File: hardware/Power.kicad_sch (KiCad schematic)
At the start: 24 parts, among them J200 Conn_Receptacle_2P, Q200 AO3401A, U200 RT9080-33GJ5, U201 TPS61023DRLR, U202 MCP73831-2-OT, X200 12401598E4#2A

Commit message: Add buttons to PCB layout
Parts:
- added SW200, SW201: SW_Push_Dual, SMD_SW_6mm:SW_Push_1P1T_NO_6x6mm_H9.5mm, symbol Switch:SW_Push_Dual
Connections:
- net GND: now also SW200.1, SW200.3, SW201.1, SW201.3
- new net JOY_BACK: SW200.2, SW200.4
- new net JOY_HOME: SW201.2, SW201.4
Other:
- note added: "User input"
- moved on the sheet: C205, R208, U202

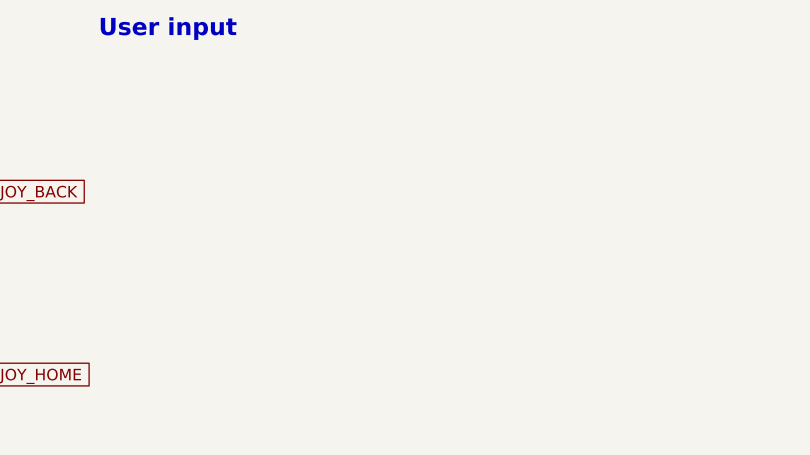
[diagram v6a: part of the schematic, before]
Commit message: Add joystick to PCB
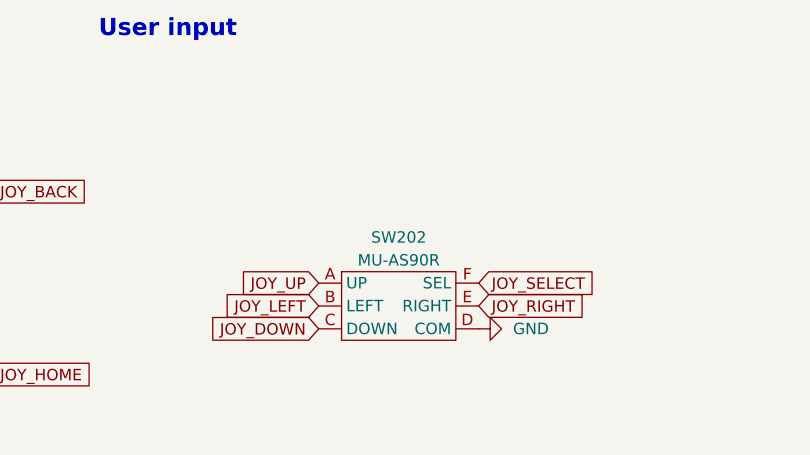
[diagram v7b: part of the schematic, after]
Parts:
- added SW202: MU-AS90R, MU-AS90R:MU-AS90R, symbol MU-AS90R:MU-AS90R
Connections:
- net GND: now also SW202.D (COM)
- new net JOY_DOWN: SW202.C (DOWN)
- new net JOY_LEFT: SW202.B (LEFT)
- new net JOY_RIGHT: SW202.E (RIGHT)
- new net JOY_SELECT: SW202.F (SEL)
- new net JOY_UP: SW202.A (UP)
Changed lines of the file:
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@@
 		)
 	)
+	(global_label "JOY_RIGHT"
+		(shape input)
+		(at 104.14 173.99 0)
+		(fields_autoplaced yes)
+		(effects
+			(font
+				(size 1.27 1.27)
+			)
+			(justify left)
+		)
+		(property "Intersheetrefs" "${INTERSHEET_REFS}"
+			(at 116.9224 173.99 0)
+			(effects
+				(font
+					(size 1.27 1.27)
+				)
+				(justify left)
+				(hide yes)
+			)
+		)
+	)
 	(global_label "JOY_BACK"
 		(shape input)
@@
 		)
 	)
+	(global_label "JOY_LEFT"
+		(shape input)
+		(at 86.36 173.99 180)
+		(fields_autoplaced yes)
+		(effects
+			(font
+				(size 1.27 1.27)
+			)
+			(justify right)
+		)
+		(property "Intersheetrefs" "${INTERSHEET_REFS}"
+			(at 86.36 173.99 0)
+			(effects
+				(font
+					(size 1.27 1.27)
+				)
+				(hide yes)
+			)
+		)
+	)
 	(global_label "USB_D-"
 		(shape input)
@@
 		)
 	)
+	(global_label "JOY_DOWN"
+		(shape input)
+		(at 86.36 176.53 180)
+		(fields_autoplaced yes)
+		(effects
+			(font
+				(size 1.27 1.27)
+			)
+			(justify right)
+		)
+		(property "Intersheetrefs" "${INTERSHEET_REFS}"
+			(at 86.36 176.53 0)
+			(effects
+				(font
+					(size 1.27 1.27)
+				)
+				(hide yes)
+			)
+		)
+	)
 	(global_label "5V_EN"
 		(shape input)
@@
 		)
 	)
+	(global_label "JOY_UP"
+		(shape input)
+		(at 86.36 171.45 180)
+		(fields_autoplaced yes)
+		(effects
+			(font
+				(size 1.27 1.27)
+			)
+			(justify right)
+		)
+		(property "Intersheetrefs" "${INTERSHEET_REFS}"
+			(at 86.36 171.45 0)
+			(effects
+				(font
+					(size 1.27 1.27)
+				)
+				(hide yes)
+			)
+		)
+	)
+	(global_label "JOY_SELECT"
+		(shape input)
+		(at 104.14 171.45 0)
+		(fields_autoplaced yes)
+		(effects
+			(font
+				(size 1.27 1.27)
+			)
+			(justify left)
+		)
+		(property "Intersheetrefs" "${INTERSHEET_REFS}"
+			(at 104.14 171.45 0)
+			(effects
+				(font
+					(size 1.27 1.27)
+				)
+				(hide yes)
+			)
+		)
+	)
 	(global_label "USB_D-"
 		(shape input)
@@
 	)
 	(symbol
+		(lib_id "MU-AS90R:MU-AS90R")
+		(at 95.25 166.37 0)
+		(unit 1)
+		(exclude_from_sim no)
+		(in_bom yes)
+		(on_board yes)
+		(dnp no)
+		(fields_autoplaced yes)
+		(property "Reference" "SW202"
+			(at 95.25 166.37 0)
+			(effects
+				(font
+					(size 1.27 1.27)
+				)
+			)
+		)
+		(property "Value" "MU-AS90R"
+			(at 95.25 168.91 0)
+			(effects
+				(font
+					(size 1.27 1.27)
+				)
+			)
+		)
+		(property "Footprint" "MU-AS90R:MU-AS90R"
+			(at 95.25 166.37 0)
+			(effects
+				(font
+					(size 1.27 1.27)
+				)
+				(hide yes)
+			)
+		)
+		(property "Datasheet" ""
+			(at 95.25 166.37 0)
+			(effects
+				(font
+					(size 1.27 1.27)
+				)
+				(hide yes)
+			)
+		)
+		(property "Description" ""
+			(at 95.25 166.37 0)
+			(effects
+				(font
+					(size 1.27 1.27)
+				)
+				(hide yes)
+			)
+		)
+		(pin "F"
+		)
+		(pin "E"
+		)
+		(pin "A"
+		)
+		(pin "D"
+		)
+		(pin "C"
+		)
+		(pin "B"
+		)
+		(instances
+			(project ""
+				(path "/da54d175-8762-4f8c-be46-30694592bf7b/f250b6aa-fac8-4faa-af78-57e6d3c4eae4"
+					(reference "SW202")
+					(unit 1)
+				)
+			)
+		)
+	)
+	(symbol
 		(lib_id "power:GND")
 		(at 60.325 55.88 90)
@@
 					(unit 1)
 				)
+			)
+		)
+	)
+	(symbol
+		(lib_name "GND_5")
+		(lib_id "power:GND")
+		(at 104.14 176.53 90)
+		(unit 1)
+		(exclude_from_sim no)
+		(in_bom yes)
+		(on_board yes)
+		(dnp no)
+		(fields_autoplaced yes)
+		(property "Reference" "#PWR0203"
+			(at 110.49 176.53 0)
+			(effects
+				(font
+					(size 1.27 1.27)
+				)
+				(hide yes)
+			)
+		)
+		(property "Value" "GND"
+			(at 107.95 176.5299 90)
+			(effects
+				(font
+					(size 1.27 1.27)
+				)
+				(justify right)
+			)
+		)
+		(property "Footprint" ""
+			(at 104.14 176.53 0)
+			(effects
+				(font
+					(size 1.27 1.27)
+				)
+				(hide yes)
+			)
+		)
+		(property "Datasheet" ""
+			(at 104.14 176.53 0)
+			(effects
+				(font
+					(size 1.27 1.27)
+				)
+				(hide yes)
+			)
+		)
+		(property "Description" "Power symbol creates a global label with name \"GND\" , ground"
+			(at 104.14 176.53 0)
+			(effects
+				(font
+					(size 1.27 1.27)
+				)
+				(hide yes)
+			)
+		)
+		(pin "1"
+		)
+		(instances
+			(project "DigiCron"
+				(path "/da54d175-8762-4f8c-be46-30694592bf7b/f250b6aa-fac8-4faa-af78-57e6d3c4eae4"
+					(reference "#PWR0203")
+					(unit 1)
+				)

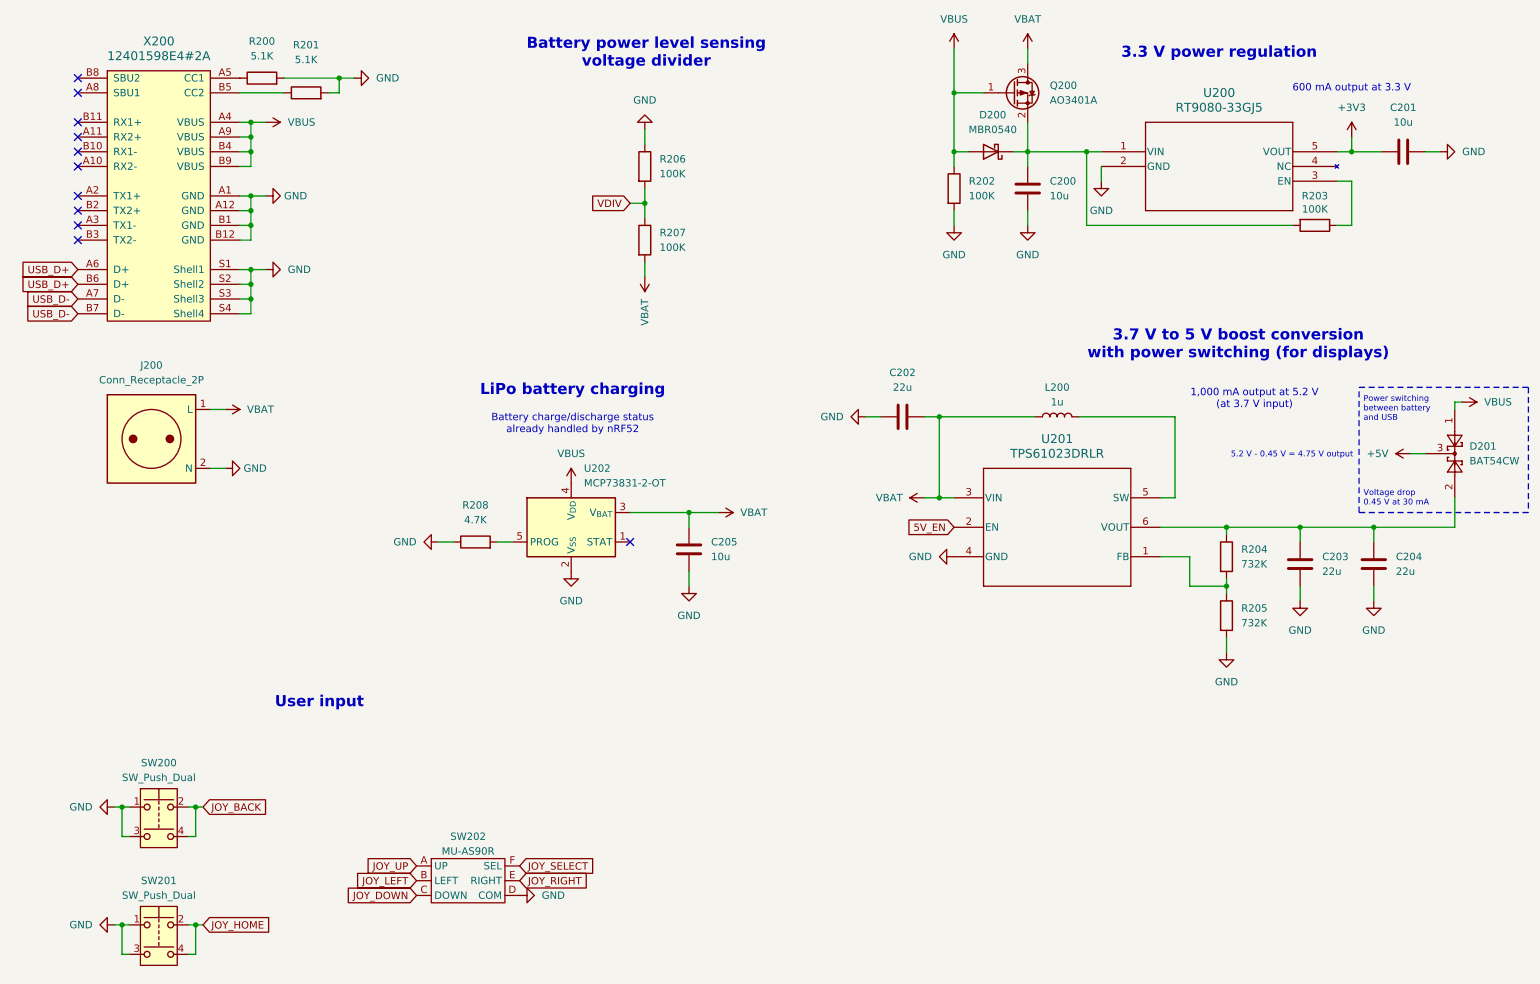
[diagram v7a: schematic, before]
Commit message: Add programming pins to PCB
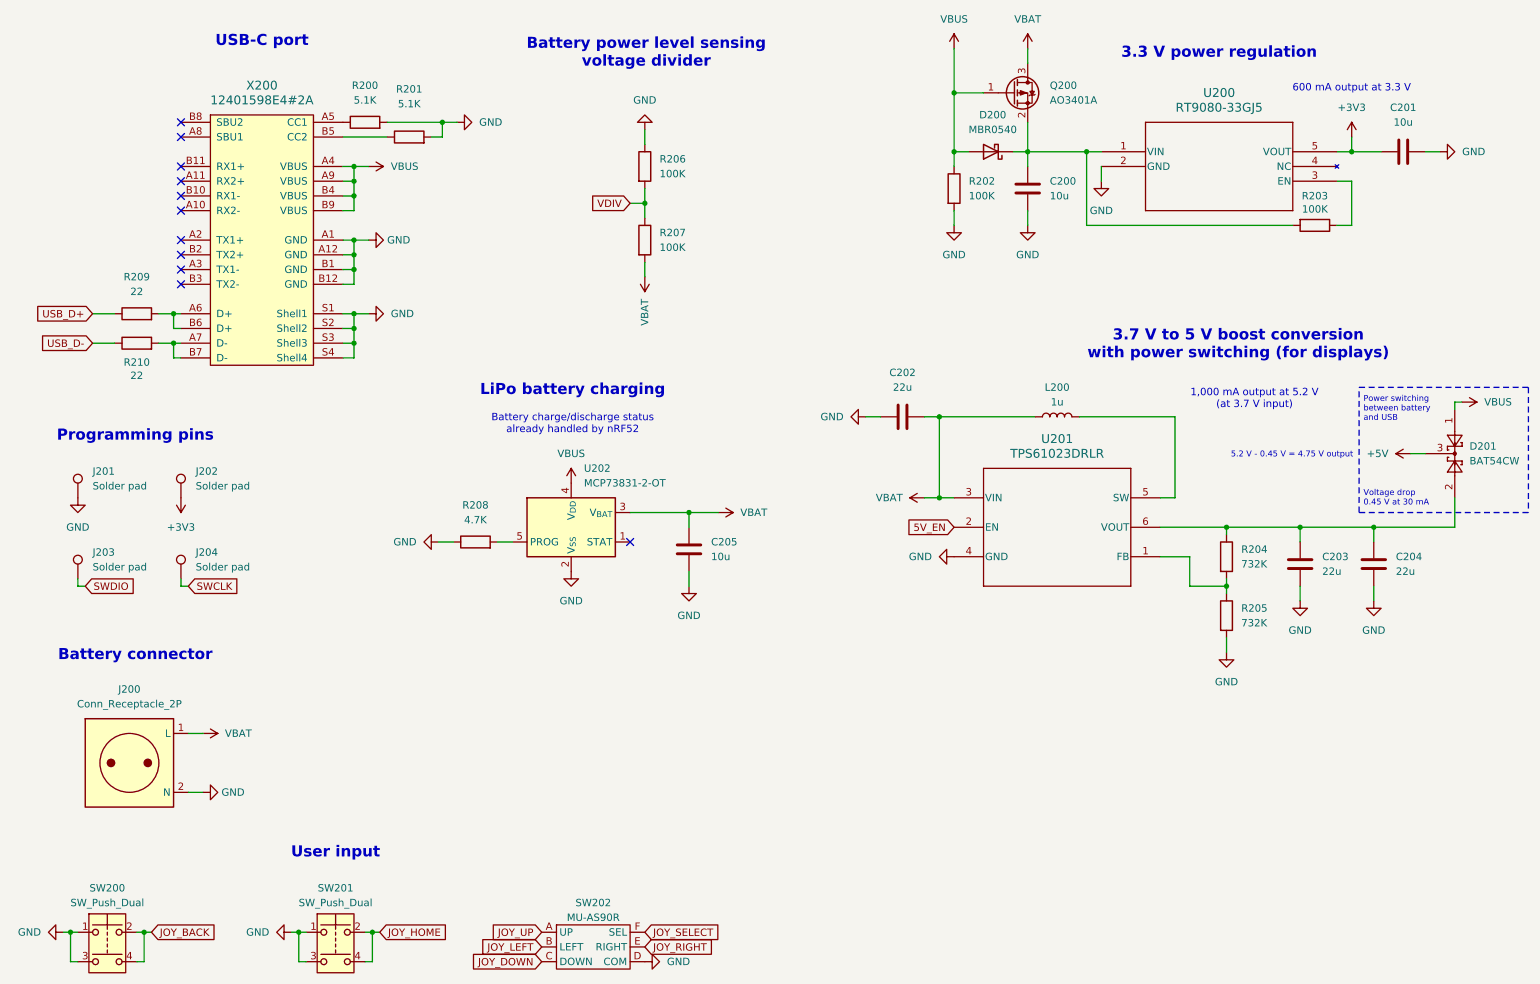
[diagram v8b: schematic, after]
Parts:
- added J201, J202, J203, J204: Solder pad, TestPoint:TestPoint_Pad_2.0x2.0mm, symbol Connector:TestPoint
- added R209, R210: 22, Resistor_SMD:R_0201_0603Metric_Pad0.64x0.40mm_HandSolder, symbol Device:R
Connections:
- net +3V3: now also J202.1
- net GND: now also J201.1
- net USB_D+: now also R209.1; no longer X200.A6 (D+), X200.B6 (D+)
- net USB_D-: now also R210.1; no longer X200.A7 (D-), X200.B7 (D-)
- new net: R210.2, X200.A7 (D-), X200.B7 (D-)
- new net: R209.2, X200.A6 (D+), X200.B6 (D+)
- new net SWCLK: J204.1
- new net SWDIO: J203.1
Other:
- note added: "Battery connector"
- note added: "Programming pins"
- note added: "USB-C port"
- moved on the sheet: J200, R200, R201, SW200, SW201, SW202, X200
